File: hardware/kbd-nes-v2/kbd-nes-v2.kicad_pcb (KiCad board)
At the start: 4 copper layers, 51.1 x 40.7 mm, 53 parts, among them J1 Conn_01x05, J2 Conn_01x02, J4 USB_C_Receptacle_USB2.0_16P, J5 Conn_01x05, J7 SM03B-SRSS-TB, Q1 2N7002, SW1 SS12D07VG6 087, U1 TPS2553DBVR, U2 W25Q128JVS, U3 RP2040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

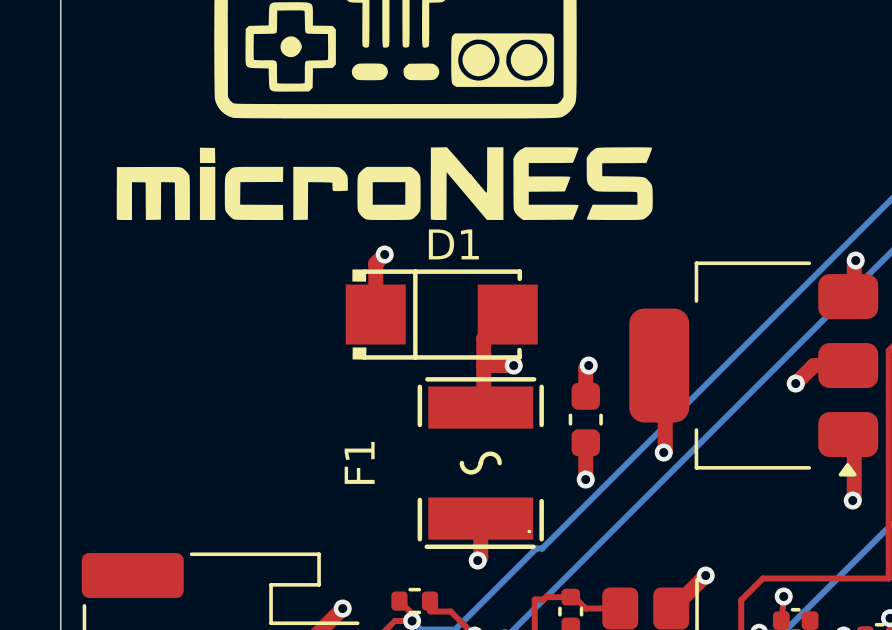
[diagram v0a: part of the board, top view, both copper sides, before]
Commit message: Add key bindings reset - need to test - and also fix schematic and PCB for diode
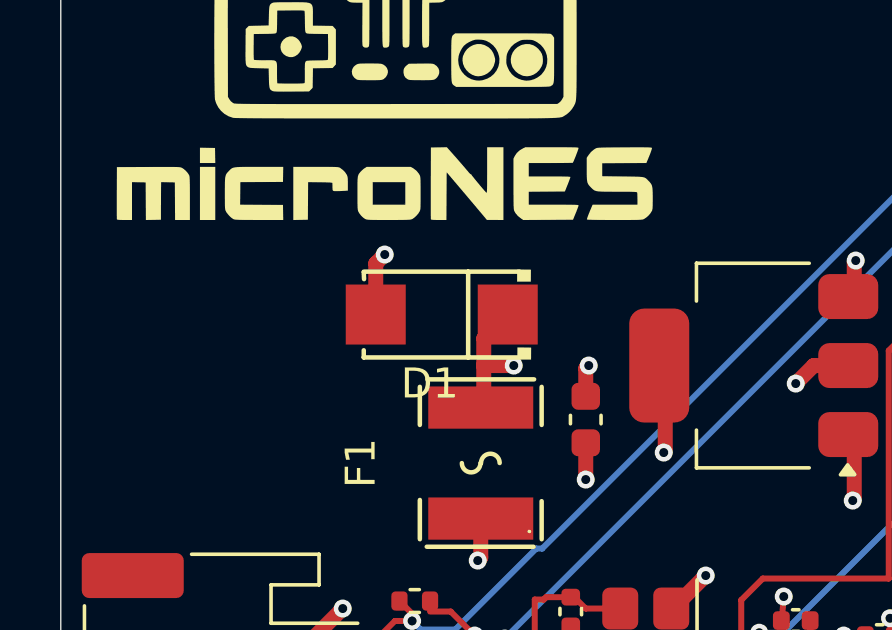
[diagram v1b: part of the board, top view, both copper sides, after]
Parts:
- turned D1 to 180 degrees
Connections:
- D1 pad 1: GND -> /NES Input Output/NES_5V_CLEAN
- D1 pad 2: /NES Input Output/NES_5V_CLEAN -> GND
